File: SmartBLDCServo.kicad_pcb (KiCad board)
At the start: 2 copper layers, 69.2 x 58.3 mm, 24 parts, among them J1 TTL Half Duplex, J2 AS5600, J3 Stepper, U1 ESP32-C3-SuperMini, U2 TMC2209_SILENTSTEPSTICK, U3 MP1584EN_8Pin_Module, U4 BOB-12009

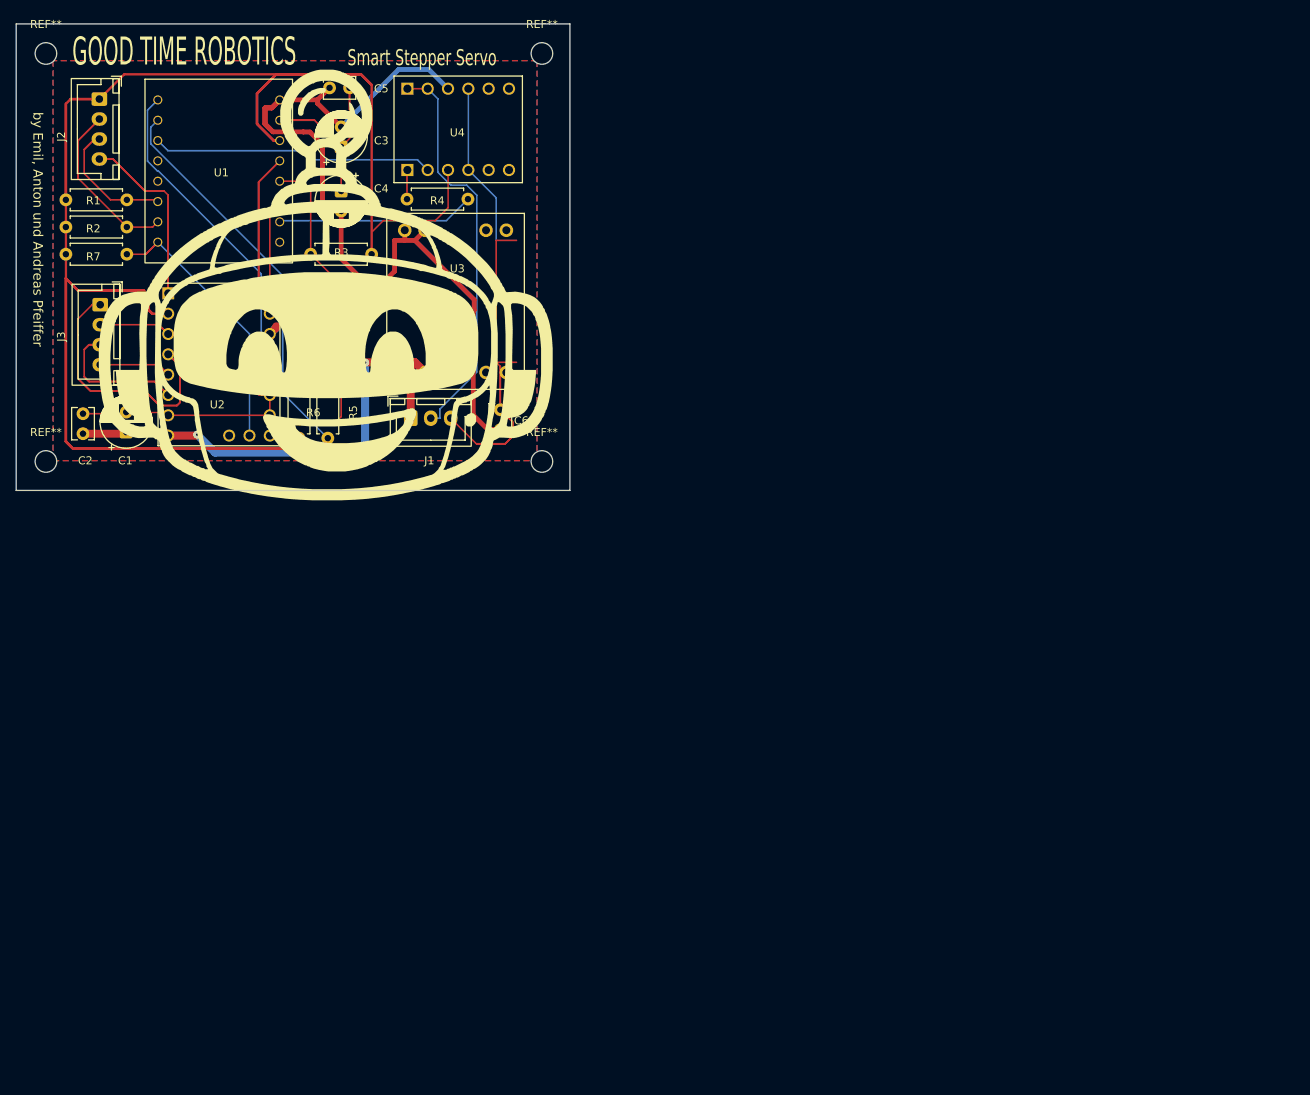
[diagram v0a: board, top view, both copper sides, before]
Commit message: Update KiCad PCB and schematic: Fix footprint UUIDs, add SimpleFOC and MP1584EN footprints
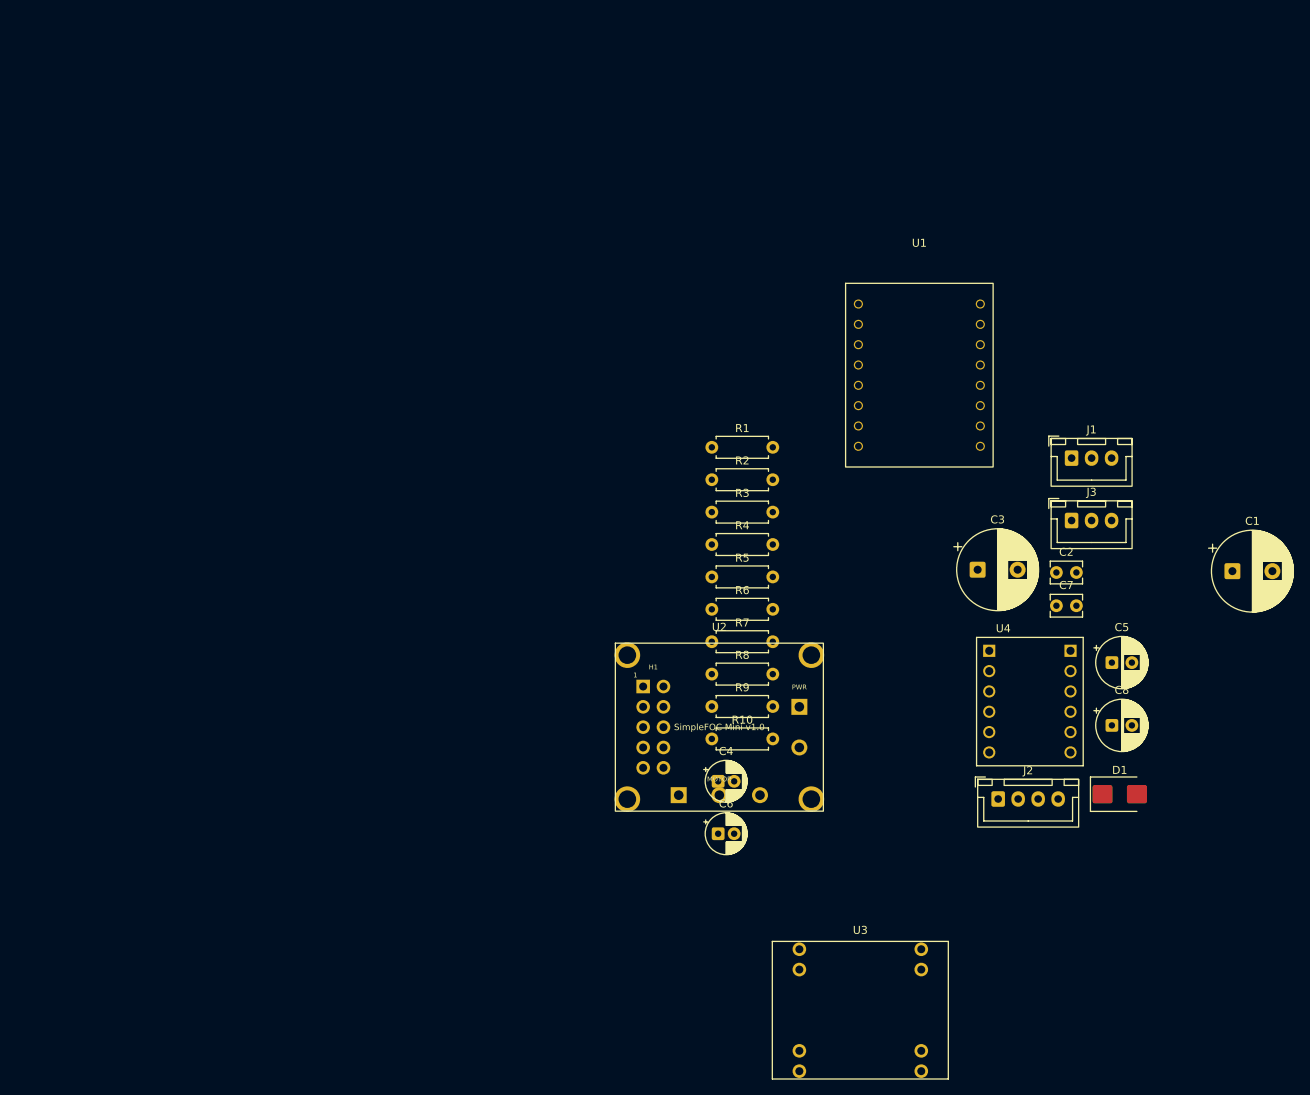
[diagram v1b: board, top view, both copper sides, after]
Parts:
- removed REF** (x4): MountingHole_2.7mm_M2.5, MountingHole:MountingHole_2.7mm_M2.5
- added C7: 100nF, Capacitor_THT:C_Disc_D3.8mm_W2.6mm_P2.50mm, F.Cu at (142.1, 84.8)
- added C8: 10uF, Capacitor_THT:CP_Radial_D6.3mm_P2.50mm, F.Cu at (149.1, 99.8)
- added D1: SMBJ15A, Diode_SMD:D_SMB, F.Cu at (150.0, 108.4)
- added R10: 2.2k, Resistor_THT:R_Axial_DIN0207_L6.3mm_D2.5mm_P7.62mm_Horizontal, F.Cu at (99.1, 101.5)
- added R8: 4.7k, Resistor_THT:R_Axial_DIN0207_L6.3mm_D2.5mm_P7.62mm_Horizontal, F.Cu at (99.1, 93.4)
- added R9: 10k, Resistor_THT:R_Axial_DIN0207_L6.3mm_D2.5mm_P7.62mm_Horizontal, F.Cu at (99.1, 97.4)
- C1: value 470uF -> 1000uF; footprint Capacitor_THT:CP_Radial_D6.3mm_P2.50mm -> Capacitor_THT:CP_Radial_D10.0mm_P5.00mm
- C3: value 100uF -> 10uF; footprint Capacitor_THT:CP_Radial_D6.3mm_P2.50mm -> Capacitor_THT:CP_Radial_D10.0mm_P5.00mm
- C4: value 47uF -> 22uF; footprint Capacitor_THT:CP_Radial_D6.3mm_P2.50mm -> Capacitor_THT:CP_Radial_D5.0mm_P2.00mm
- C5: value 100nF -> 100uF; footprint Capacitor_THT:C_Disc_D3.8mm_W2.6mm_P2.50mm -> Capacitor_THT:CP_Radial_D6.3mm_P2.50mm
- C6: value 22uF -> 47uF; footprint Capacitor_THT:C_Disc_D3.8mm_W2.6mm_P2.50mm -> Capacitor_THT:CP_Radial_D5.0mm_P2.00mm
- J3: value Stepper -> BLDC; footprint Connector_JST:JST_XH_B4B-XH-A_1x04_P2.50mm_Vertical -> Connector_JST:JST_XH_B3B-XH-A_1x03_P2.50mm_Vertical
- R1, R2: value 4.7k -> 10k
- R4: value 220 -> 10k
- R5: value 1k -> 4.7k
- R7: value 4.7k -> 220
- U2: value TMC2209_SILENTSTEPSTICK -> SimpleFOC_Mini_v1_0; footprint TMC2209_SILENTSTEPSTICK:MODULE_TMC2209_SILENTSTEPSTICK -> simplefoc_mini:SimpleFOC_Mini_v1_0
- U3: footprint SmartServo_V2_Custom:MP1584EN_8Pin_Module -> MP1584EN_8Pin_Module
- moved J2 142.4 mm to (134.8, 109.0), turned to 0 degrees
- moved C1 139.4 mm to (164.1, 80.5), turned to 0 degrees
- moved J3 124.4 mm to (144.0, 74.2), turned to 0 degrees
- moved C2 122.9 mm to (142.1, 80.7), turned to 0 degrees
- moved C5 119.3 mm to (149.1, 91.9), turned to 0 degrees
- moved U3 102.0 mm to (117.6, 135.4), turned to 0 degrees
- moved U4 101.1 mm to (138.8, 96.8), turned to 0 degrees
- moved C3 95.5 mm to (132.3, 80.3), turned to 0 degrees
- moved U1 91.2 mm to (125.0, 56.0)
- moved R7 87.7 mm to (99.1, 89.3), turned to 0 degrees
- moved C4 87.5 mm to (99.8, 106.8), turned to 0 degrees
- moved J1 82.8 mm to (144.0, 66.4)
- moved R2 79.7 mm to (99.1, 69.1), turned to 0 degrees
- moved R1 79.4 mm to (99.1, 65.0), turned to 0 degrees
- moved U2 77.2 mm to (100.0, 100.0)
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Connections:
- C2 pad 1: +12V -> GND
- C2 pad 2: GND -> +12V
- C3 pad 1: GND -> +12V
- C3 pad 2: +5V -> GND
- C4 pad 1: GND -> +5V
- C4 pad 2: +5V -> GND
- C5 pad 1: GND -> +5V
- C5 pad 2: +5V -> GND
- J3 pad 1: /M1A -> /A
- J3 pad 2: /M1B -> /B
- J3 pad 3: /M2A -> /C
- R1 pad 1: /I2C_SCL -> /FOC_EN
- R1 pad 2: +3.3V -> GND
- R2 pad 1: /I2C_SDA -> /FOC_nFLT
- R3 pad 1: /TMC_EN -> Net-(U2-nSLP)
- R4 pad 1: Net-(R4-Pad1) -> Net-(U2-nRST)
- R4 pad 2: /FT_TX -> +3.3V
- R5 pad 1: /TMC_RX -> /I2C_SDA
- R5 pad 2: /TMC_TX -> +3.3V
- R6 pad 1: /TMC_RX -> /I2C_SCL
- R7 pad 1: /TMC_DIAG -> Net-(R7-Pad1)
- R7 pad 2: +3.3V -> /FT_TX
- U1 pad 1: unconnected-(U1-GPIO0-Pad1) -> /FOC_IN1
- U1 pad 10: /TMC_TX -> unconnected-(U1-GPIO6-Pad10)
- U1 pad 11: /FT_RX -> unconnected-(U1-GPIO7-Pad11)
- U1 pad 12: unconnected-(U1-GPIO8-Pad12) -> /I2C_SDA
- U1 pad 13: unconnected-(U1-GPIO9-Pad13) -> /I2C_SCL
- U1 pad 14: /I2C_SCL -> unconnected-(U1-GPIO10-Pad14)
- U1 pad 15: /I2C_SDA -> /FT_RX
- U1 pad 16: /TMC_DIAG -> /FT_TX
- U1 pad 2: /FT_TX -> /FOC_IN2
- U1 pad 3: /TMC_DIR -> /FOC_IN3
- U1 pad 4: /TMC_EN -> /FOC_EN
- U1 pad 5: /TMC_STEP -> /FOC_nFLT
- U1 pad 9: /TMC_RX -> unconnected-(U1-GPIO5-Pad9)
- U2 pad 10: /TMC_STEP -> /FOC_nFLT
- U2 pad 11: GND -> /C
- U2 pad 12: GND -> /B
- U2 pad 13: /TMC_RX -> /A
- U2 pad 14: GND -> +12V
- U2 pad 16: /TMC_EN -> (no net)
- U2 pad 17: unconnected-(U2-INDEX-Pad17) -> (no net)
- U2 pad 18: /TMC_DIAG -> (no net)
- U2 pad 2: +3.3V -> unconnected-(U2-3.3V-Pad2)
- U2 pad 3: /M1B -> /FOC_IN1
- U2 pad 4: /M1A -> GND
- U2 pad 5: /M2B -> /FOC_IN2
- U2 pad 6: /M2A -> Net-(U2-nRST)
- U2 pad 7: GND -> /FOC_IN3
- U2 pad 8: +12V -> Net-(U2-nSLP)
- U2 pad 9: /TMC_DIR -> /FOC_EN
- U4 pad HV2: /TTL_1_Wire -> unconnected-(U4-PadHV2)
- U4 pad LV1: Net-(R4-Pad1) -> Net-(R7-Pad1)
- U4 pad LV2: /FT_RX -> unconnected-(U4-PadLV2)
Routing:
- net +3.3V: track 277.1 -> 0.00 mm
- net GND: track 200.2 -> 0.00 mm
- net +5V: track 120.1 -> 0.00 mm
- net +12V: track 63.9 -> 0.00 mm, vias 2 -> 0
- net /M1A: track 53.9 -> 0.00 mm
- net /TTL_1_Wire: track 50.5 -> 0.00 mm
- net /TMC_TX: track 49.3 -> 0.00 mm
- net /TMC_RX: track 49.1 -> 0.00 mm
- net /TMC_EN: track 44.1 -> 0.00 mm
- net /TMC_STEP: track 39.6 -> 0.00 mm
- net /TMC_DIAG: track 35.6 -> 0.00 mm
- net /FT_RX: track 35.3 -> 0.00 mm
- net /M2A: track 32.1 -> 0.00 mm
- net /I2C_SDA: track 29.8 -> 0.00 mm
- net /FT_TX: track 24.7 -> 0.00 mm
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- removed copper zone on B.Cu, net GND
- removed copper zone on F.Cu, net GND
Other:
- board outline removed
- board text removed: "GOOD TIME ROBOTICS"
- board text removed: "Smart Stepper Servo"
- board text removed: "by Emil, Anton und Andreas Pfeiffer"
